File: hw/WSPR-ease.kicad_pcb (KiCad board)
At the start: 4 copper layers, 99 x 64 mm, 123 parts, among them J101 GNSS Ant, J102 Tx Ant, J103 pwr+data, Q101 MMBF170, Q301 MMBF170, Q302 MMBF170, Q303 MMBF170, Q304 MMBF170, Q305 MMBF170, Q306 MMBF170, Q307 MMBF170, Q308 MMBF170, Q309 MMBF170, Q310 MMBF170, Q311 MMBF170, Q312 MMBF170, T301 BN-43-202_DualPri_CTSec, U101 ATGM336H-5N31, U102 ESP32-S3-WROOM-1-N8R8, U103 TPS22918DBVR, U104 TPS74612PQWDRBRQ1, U105 SRV05-4, U106 LMR51430, U201 AS183-92LF, U202 AS183-92LF, U203 AS183-92LF, U204 AS183-92LF, U301 ICE40UP5K-SG48ITR, U302 CD74ACT541SM96, Y301 40MHz

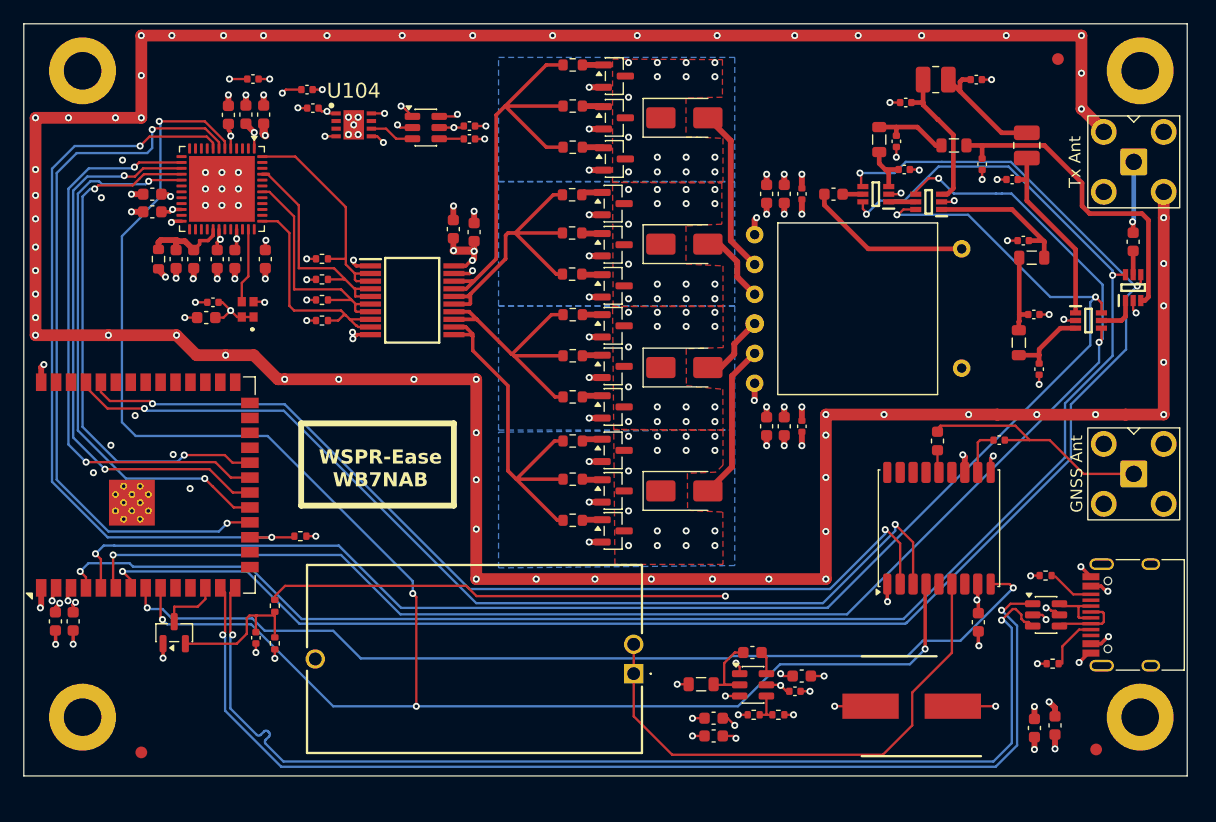
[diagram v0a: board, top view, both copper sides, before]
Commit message: Clean up some clearances found by FlashPCB tools
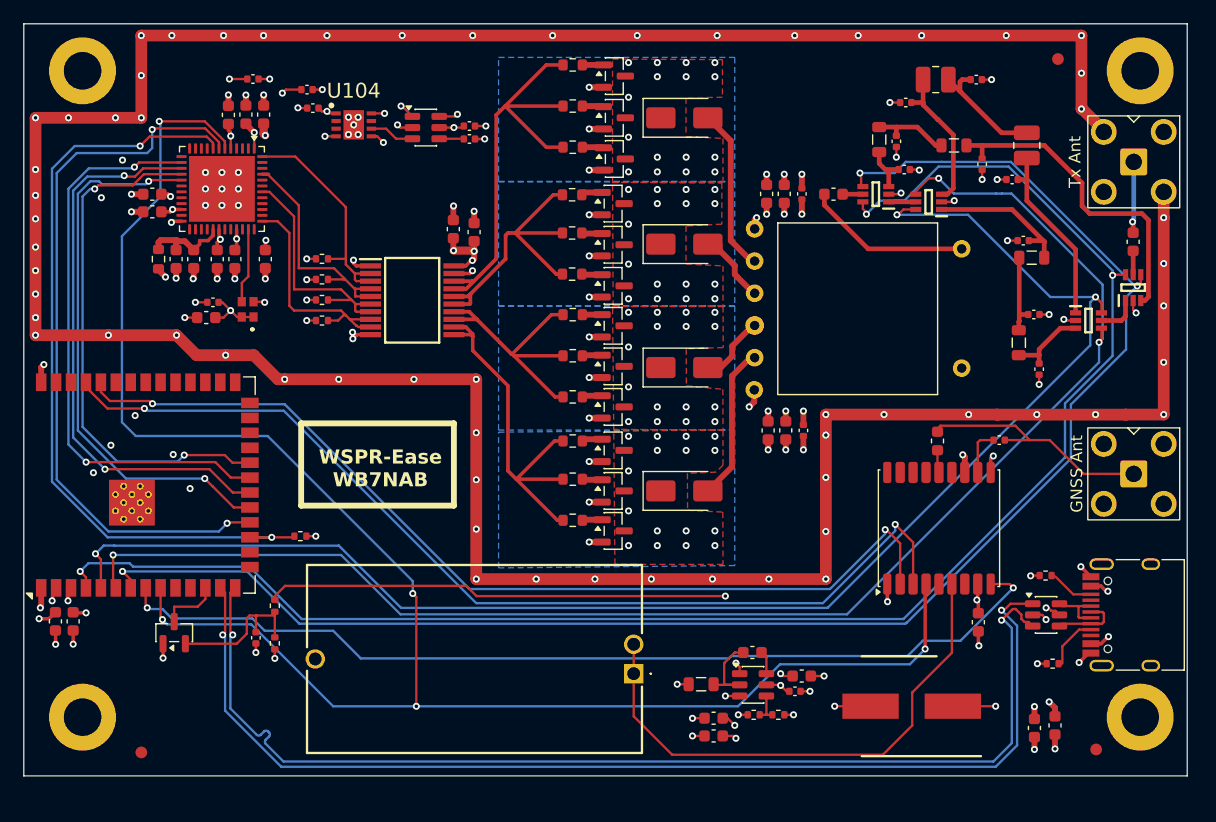
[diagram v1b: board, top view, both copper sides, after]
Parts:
- moved C316 0.38 mm to (112.9, 104.0)
- moved C318 0.38 mm to (114.4, 104.0)
- moved C320 0.38 mm to (115.9, 104.0)
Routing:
- net +3.3V: track 18.0 -> 18.8 mm
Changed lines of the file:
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@@
 	(footprint "Capacitor_SMD:C_0402_1005Metric"
 		(layer "F.Cu")
-		(at 115.81 103.65 90)
+		(at 115.94 104.0025 90)
 		(descr "Capacitor SMD 0402 (1005 Metric), square (rectangular) end terminal, IPC-7351 nominal, (Body size source: IPC-SM-782 page 76, https://www.pcb-3d.com/wordpress/wp-content/uploads/ipc-sm-782a_amendment_1_and_2.pdf), generated with kicad-footprint-generator")
 		(tags "capacitor")
@@
 	(footprint "Capacitor_SMD:C_0603_1608Metric"
 		(layer "F.Cu")
-		(at 112.81 103.65 90)
+		(at 112.94 104.0025 90)
 		(descr "Capacitor SMD 0603 (1608 Metric), square (rectangular) end terminal, IPC-7351 nominal, (Body size source: IPC-SM-782 page 76, https://www.pcb-3d.com/wordpress/wp-content/uploads/ipc-sm-782a_amendment_1_and_2.pdf), generated with kicad-footprint-generator")
 		(tags "capacitor")
@@
 	(footprint "Capacitor_SMD:C_0603_1608Metric"
 		(layer "F.Cu")
-		(at 114.31 103.65 90)
+		(at 114.44 104.0025 90)
 		(descr "Capacitor SMD 0603 (1608 Metric), square (rectangular) end terminal, IPC-7351 nominal, (Body size source: IPC-SM-782 page 76, https://www.pcb-3d.com/wordpress/wp-content/uploads/ipc-sm-782a_amendment_1_and_2.pdf), generated with kicad-footprint-generator")
 		(tags "capacitor")
@@
 		)
 		(pad "1" thru_hole circle
-			(at -6.34 -8.77 90)
+			(at -6.9 -8.8 90)
 			(size 1.5 1.5)
 			(drill 0.8)
@@
 		)
 		(pad "2" thru_hole circle
-			(at -3.8 -8.77 90)
+			(at -4.16 -8.77 90)
 			(size 1.5 1.5)
 			(drill 0.8)
@@
 		)
 		(pad "3" thru_hole circle
-			(at -1.26 -8.77 180)
+			(at -1.42 -8.77 180)
 			(size 1.6 1.6)
 			(drill 0.8)
@@
 		)
 		(pad "4" thru_hole circle
-			(at 1.23 -8.77 90)
+			(at 1.32 -8.77 90)
 			(size 1.5 1.5)
 			(drill 0.8)
@@
 		)
 		(pad "5" thru_hole circle
-			(at 3.77 -8.77 180)
+			(at 4.06 -8.77 180)
 			(size 1.5 1.5)
 			(drill 0.8)
@@
 		)
 		(pad "6" thru_hole circle
-			(at 6.31 -8.77 90)
+			(at 6.8 -8.77 90)
 			(size 1.5 1.5)
 			(drill 0.8)
@@
 	)
 	(segment
-		(start 114.31 104.425)
-		(end 114.31 105.3)
+		(start 114.44 104.7775)
+		(end 114.44 105.6525)
 		(width 0.5)
 		(layer "F.Cu")
@@
 	)
 	(segment
-		(start 115.81 104.425)
-		(end 115.81 105.3)
+		(start 115.94 104.7775)
+		(end 115.94 105.6525)
 		(width 0.5)
 		(layer "F.Cu")
@@
 	)
 	(segment
-		(start 112.81 104.425)
-		(end 112.81 105.3)
+		(start 112.94 104.7775)
+		(end 112.94 105.6525)
 		(width 0.5)
 		(layer "F.Cu")
@@
 	)
 	(via
-		(at 114.31 105.3)
+		(at 114.44 105.6525)
 		(size 0.6)
 		(drill 0.3)
@@
 	)
 	(via
-		(at 115.81 105.3)
+		(at 115.94 105.6525)
 		(size 0.6)
 		(drill 0.3)
@@
 	)
 	(via
-		(at 112.81 105.3)
+		(at 112.94 105.6525)
 		(size 0.6)
 		(drill 0.3)
@@
 	)
 	(segment
+		(start 53.85 119.525)
+		(end 53.8 119.475)
+		(width 0.3)
+		(layer "F.Cu")
+		(net 2)
+	)
+	(segment
 		(start 62.26 86.2)
 		(end 62.16 86.3)
@@
 	)
 	(segment
+		(start 54.9 119.525)
+		(end 53.85 119.525)
+		(width 0.3)
+		(layer "F.Cu")
+		(net 2)
+	)
+	(segment
 		(start 136.771766 119.099)
 		(end 137.022766 119.35)
@@
 	)
 	(segment
-		(start 52.29 119.07)
-		(end 52.66 118.7)
-		(width 0.3)
-		(layer "F.Cu")
-		(net 2)
-	)
-	(segment
 		(start 136.588734 119.099)
 		(end 136.771766 119.099)
@@
 	)
 	(segment
-		(start 82.6725 77.28)
-		(end 81.7925 76.4)
-		(width 0.2)
+		(start 51.74 120.025)
+		(end 52.29 119.475)
+		(width 0.3)
 		(layer "F.Cu")
 		(net 2)
 	)
 	(segment
-		(start 53.8 118.828896)
-		(end 54.001466 118.62743)
-		(width 0.3)
+		(start 82.6725 77.28)
+		(end 81.7925 76.4)
+		(width 0.2)
 		(layer "F.Cu")
 		(net 2)
@@
 	)
 	(segment
-		(start 52.29 119.475)
-		(end 52.29 119.07)
-		(width 0.3)
-		(layer "F.Cu")
-		(net 2)
-	)
-	(segment
 		(start 52.06 118.45)
 		(end 52.01 118.5)
@@
 	)
 	(segment
-		(start 53.8 119.475)
-		(end 53.8 118.828896)
-		(width 0.3)
-		(layer "F.Cu")
-		(net 2)
-	)
-	(segment
 		(start 106.175 125.6)
 		(end 105.2 125.6)
@@
 		(net 2)
 	)
+	(segment
+		(start 50.9 120.025)
+		(end 51.74 120.025)
+		(width 0.3)
+		(layer "F.Cu")
+		(net 2)
+	)
 	(via
 		(at 61.45 123.375)
@@
 	)
 	(via
-		(at 54.001466 118.62743)
+		(at 54.9 119.525)
 		(size 0.6)
 		(drill 0.3)
@@
 	)
 	(via
-		(at 52.66 118.7)
+		(at 50.9 120.025)
 		(size 0.6)
 		(drill 0.3)
@@
 	)
 	(segment
+		(start 111.76 100.55)
+		(end 111.76 101.565)
+		(width 0.5)
+		(layer "F.Cu")
+		(net 3)
+	)
+	(segment
 		(start 137.35 127.6)
 		(end 136.85 127.1)
@@
 	)
 	(segment
+		(start 111.76 101.565)
+		(end 111.325 102)
+		(width 0.5)
+		(layer "F.Cu")
+		(net 3)
+	)
+	(segment
 		(start 135.6 128.55)
 		(end 135.6 127.5)
@@
 	)
 	(segment
-		(start 114.31 102.875)
-		(end 114.31 102)
+		(start 114.44 103.2275)
+		(end 114.44 102.3525)
 		(width 0.5)
 		(layer "F.Cu")
@@
 	)
 	(segment
-		(start 115.81 102.875)
-		(end 115.81 102)
-		(width 0.5)
-		(layer "F.Cu")
-		(net 3)
-	)
-	(segment
-		(start 111.79 99.99)
-		(end 111.79 101.42)
+		(start 115.94 103.2275)
+		(end 115.94 102.3525)
 		(width 0.5)
 		(layer "F.Cu")
@@
 	)
 	(segment
-		(start 112.81 102.875)
-		(end 112.81 102)
+		(start 112.94 103.2275)
+		(end 112.94 102.3525)
 		(width 0.5)
 		(layer "F.Cu")
@@
 	)
 	(segment
-		(start 111.79 101.42)
-		(end 111.76 101.45)
-		(width 0.5)
-		(layer "F.Cu")
-		(net 3)
-	)
-	(segment
 		(start 128.8525 127.47)
 		(end 132.3 127.47)
@@
 	)
 	(via
-		(at 112.81 102)
+		(at 112.94 102.3525)
 		(size 0.6)
 		(drill 0.3)
@@
 	)
 	(via
-		(at 114.31 102)
+		(at 114.44 102.3525)
 		(size 0.6)
 		(drill 0.3)
@@
 	)
 	(via
-		(at 115.81 102)
+		(at 115.94 102.3525)
 		(size 0.6)
 		(drill 0.3)
@@
 	)
 	(via
-		(at 111.76 101.45)
+		(at 111.325 102)
 		(size 0.6)
 		(drill 0.3)
@@
 	)
 	(segment
-		(start 107.81 98.65)
-		(end 108.91 98.65)
+		(start 108.91 98.65)
+		(end 109.875 97.685)
 		(width 0.5)
 		(layer "F.Cu")
@@
 	)
 	(segment
-		(start 110.06 96.64)
+		(start 109.875 96.825)
 		(end 111.79 94.91)
 		(width 0.5)
@@
 	)
 	(segment
-		(start 110.06 97.5)
-		(end 110.06 96.64)
+		(start 109.875 97.685)
+		(end 109.875 96.825)
 		(width 0.5)
 		(layer "F.Cu")
@@
 	)
 	(segment
-		(start 108.91 98.65)
-		(end 110.06 97.5)
+		(start 107.81 98.65)
+		(end 108.91 98.65)
 		(width 0.5)
 		(layer "F.Cu")
@@
 	)
 	(segment
-		(start 110.31 89.65)
-		(end 110.31 90.94)
+		(start 110.1 89.975)
+		(end 110.1 90.725)
+		(width 0.5)
+		(layer "F.Cu")
+		(net 106)
+	)
+	(segment
+		(start 108.81 88.685)
+		(end 110.1 89.975)
 		(width 0.5)
 		(layer "F.Cu")
@@
 	(segment
 		(start 108.81 88.15)
-		(end 110.31 89.65)
+		(end 108.81 88.685)
 		(width 0.5)
 		(layer "F.Cu")
@@
 		(width 0.5)
 		(layer "F.Cu")
+		(net 106)
+	)
+	(segment
+		(start 110.1 90.725)
+		(end 110.31 90.935)
+		(width 0.5)
+		(layer "F.Cu")
+		(net 106)
+	)
+	(segment
+		(start 110.31 90.935)
+		(end 110.31 90.94)
+		(width 0.5)
+		(layer "F.Cu")

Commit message: Cleanup and prep for MacroFab quote
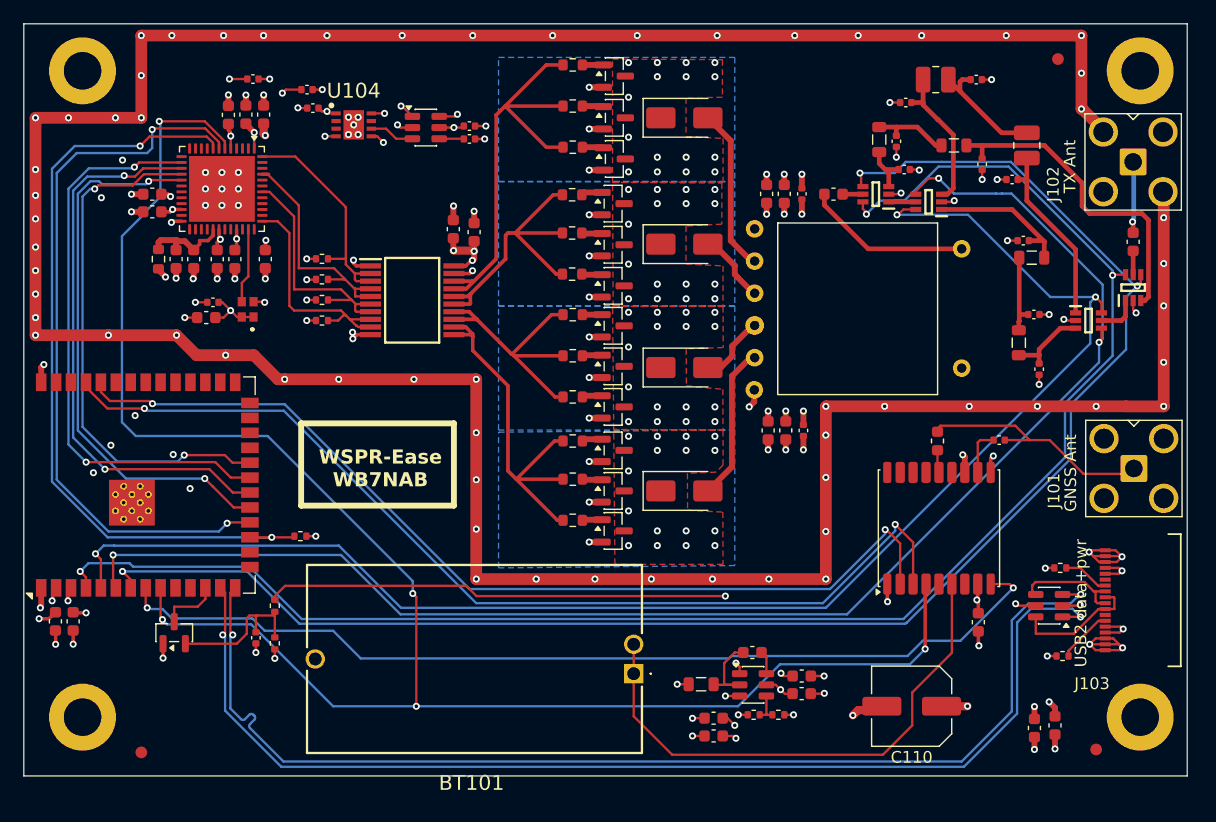
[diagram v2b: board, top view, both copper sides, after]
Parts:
- C110: renamed from C109; footprint Library:CAPAE850X1050N -> Capacitor_SMD:C_Elec_6.3x7.7
- C111: renamed from C113; value 1uF -> 1uF X7R 25V; footprint Capacitor_SMD:C_0402_1005Metric -> Capacitor_SMD:C_0603_1608Metric
- J101: value GNSS Ant -> SMA; footprint Connector_Coaxial:SMA_BAT_Wireless_BWSMA-KWE-Z001 -> Library:SMA_Amphenol_901-143_Horizontal
- J102: value Tx Ant -> SMA; footprint Connector_Coaxial:SMA_BAT_Wireless_BWSMA-KWE-Z001 -> Library:SMA_Amphenol_901-143_Horizontal
- J103: value pwr+data -> CX90M-16P; footprint Library:USB_C_Receptacle_HRO_TYPE-C-31-M-12-bursted -> Library:CX90M-16P_HIR
- U101: value ATGM336H-5N31 -> GNSS module
- U106: value LMR51430 -> LMR51430YDDCR
- moved R104 1.41 mm to (137.8, 115.7)
- moved J103 1.27 mm to (144.7, 118.5)
- moved R103 1.06 mm to (138.0, 123.2)
- moved U105 0.83 mm to (136.8, 118.9), turned to 180 degrees
- moved C111 0.60 mm to (115.8, 126.4)
- moved J101 0.46 mm to (144.1, 107.2)
- moved J102 0.05 mm to (144.0, 81.2)
- renumbered C112 to C109, C110 to C112, C111 to C113
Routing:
- net GND: track 362.4 -> 379.2 mm, vias 167 -> 169
- net Net-(U105-IO4): track 4.49 -> 10.7 mm
- net Net-(U105-IO3): track 5.51 -> 9.30 mm
- net /D-: track 95.7 -> 98.3 mm
- net /D+: track 95.8 -> 97.5 mm
- net /Transmitter/pull1T: track 5.50 -> 4.97 mm
- net VBUS: track 61.3 -> 61.6 mm, vias 17 -> 16

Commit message: Parts ordered for DVT1 build
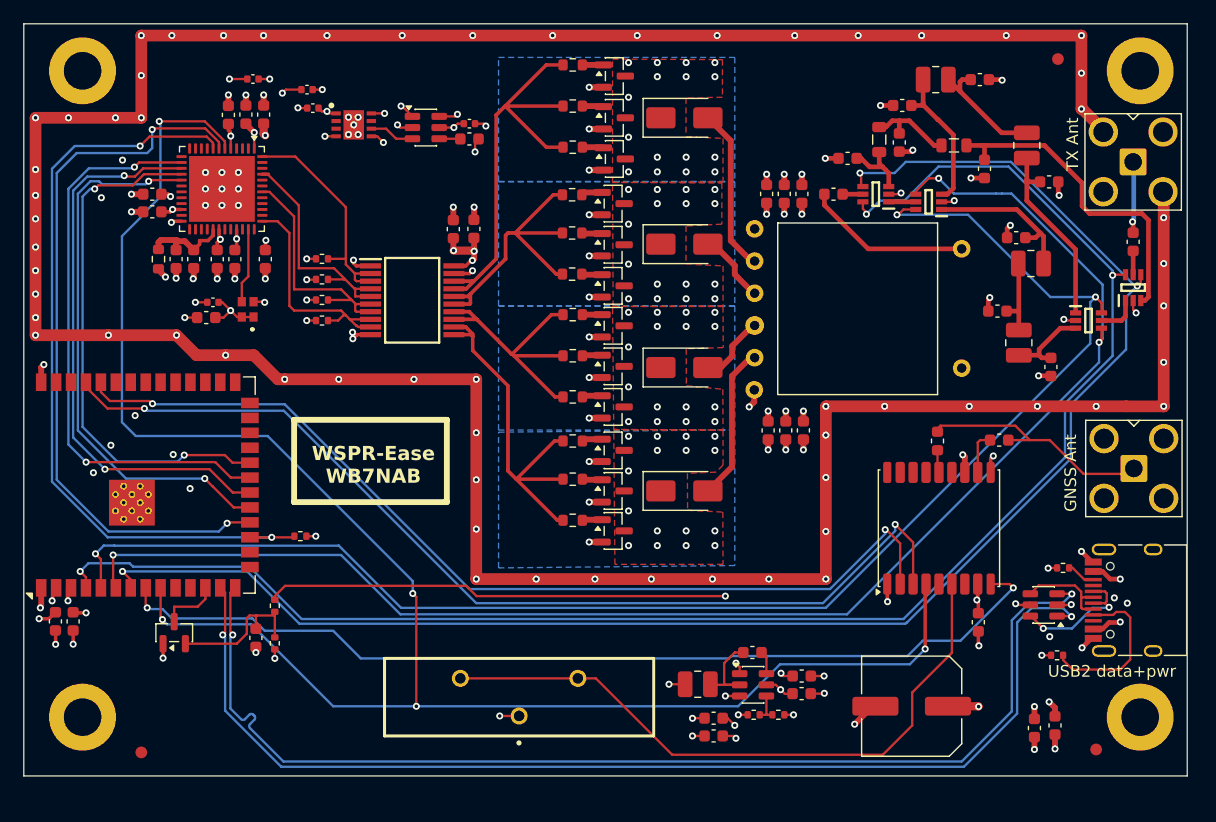
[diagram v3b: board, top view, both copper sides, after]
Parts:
- BT101: footprint Library:BATHLD014THM -> Library:S8401-46
- C102, C106: value 1nF X7R -> 1nF NP0 100V; footprint Capacitor_SMD:C_0402_1005Metric -> Capacitor_SMD:C_0603_1608Metric
- C103, C204, C210, C319, C320: value 100pF NP0 50V -> 100pF NP0 100V; footprint Capacitor_SMD:C_0402_1005Metric -> Capacitor_SMD:C_0603_1608Metric
- C110: footprint Capacitor_SMD:C_Elec_6.3x7.7 -> Capacitor_SMD:C_Elec_8x6.2
- C202, C206, C208: value 470pF NP0 -> 470pF NP0 100V; footprint Capacitor_SMD:C_0402_1005Metric -> Capacitor_SMD:C_0603_1608Metric
- C203, C207, C209: value 220pF NP0 -> 220pF NP0 100V; footprint Capacitor_SMD:C_0402_1005Metric -> Capacitor_SMD:C_0603_1608Metric
- C205: value 1nF NP0 -> 1nF NP0 100V; footprint Capacitor_SMD:C_0402_1005Metric -> Capacitor_SMD:C_0603_1608Metric
- J103: value CX90M-16P -> 640-USB4930-00-A; footprint Library:CX90M-16P_HIR -> Library:USB_C_Receptacle_HRO_TYPE-C-31-M-12-bursted
- L102, L202, L205: footprint Inductor_SMD:L_0805_2012Metric -> Inductor_SMD:L_1008_2520Metric
- moved BT101 9.95 mm to (91.8, 126.7)
- moved C204 4.91 mm to (119.7, 80.8), turned to 180 degrees
- moved C208 3.16 mm to (136.8, 82.8), turned to 0 degrees
- moved C206 3.11 mm to (132.4, 93.8), turned to 180 degrees
- moved C209 1.02 mm to (137.0, 98.6)
- moved C203 0.65 mm to (134.1, 87.6)
- moved L202 0.50 mm to (135.3, 89.8)
- moved R103 0.47 mm to (137.5, 123.1)
- moved U105 0.47 mm to (136.4, 118.8)
- moved C210 0.45 mm to (131.3, 81.8)
- moved C202 0.39 mm to (124.3, 76.3)
- moved C205 0.30 mm to (130.9, 74.2)
- moved L102 0.29 mm to (107.0, 125.6)
- moved C309 0.28 mm to (87.9, 86.8)
- moved C207 0.27 mm to (124.1, 79.5)
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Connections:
- BT101 pad 1: Net-(BT101-+_1) -> GND
- BT101 pad 2: Net-(BT101-+_1) -> Net-(BT101-+_2)
- BT101 pad 3: GND -> Net-(BT101-+_2)
- U101 pad 6: Net-(BT101-+_1) -> Net-(BT101-+_2)
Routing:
- net Net-(BT101-+_2): track 0.00 -> 55.6 mm
- net Net-(BT101-+_1): track 45.6 -> 0.00 mm
- net GND: track 379.2 -> 367.5 mm, vias 169 -> 171
- net Net-(J103-CC1): track 4.63 -> 13.8 mm
- net Net-(J103-CC2): track 3.92 -> 2.47 mm
- net Net-(U201-J3): track 4.40 -> 5.77 mm
- net /D+: track 97.5 -> 96.5 mm
- net Net-(U105-IO3): track 9.30 -> 8.28 mm
- net /D-: track 98.3 -> 97.3 mm
- net Net-(C207-Pad1): track 6.67 -> 7.46 mm
- net Net-(U202-J2): track 12.6 -> 13.4 mm
- net Net-(U105-IO4): track 10.7 -> 11.5 mm, vias 0 -> 2
- net +VFPGAIO: track 24.2 -> 24.7 mm
